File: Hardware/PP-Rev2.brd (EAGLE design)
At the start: 190.5 x 101.3 mm, 181 parts, among them IC1 LT6004, IC2 TLC6C5912-Q1, J1 J_0399700102, Q1 MOSFET-PCHANNEL, Q10 2N7002PW, Q11 2N7002PW, Q12 2N7002PW, Q13 2N7002PW, Q14 2N7002PW, Q15 2N7002PW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

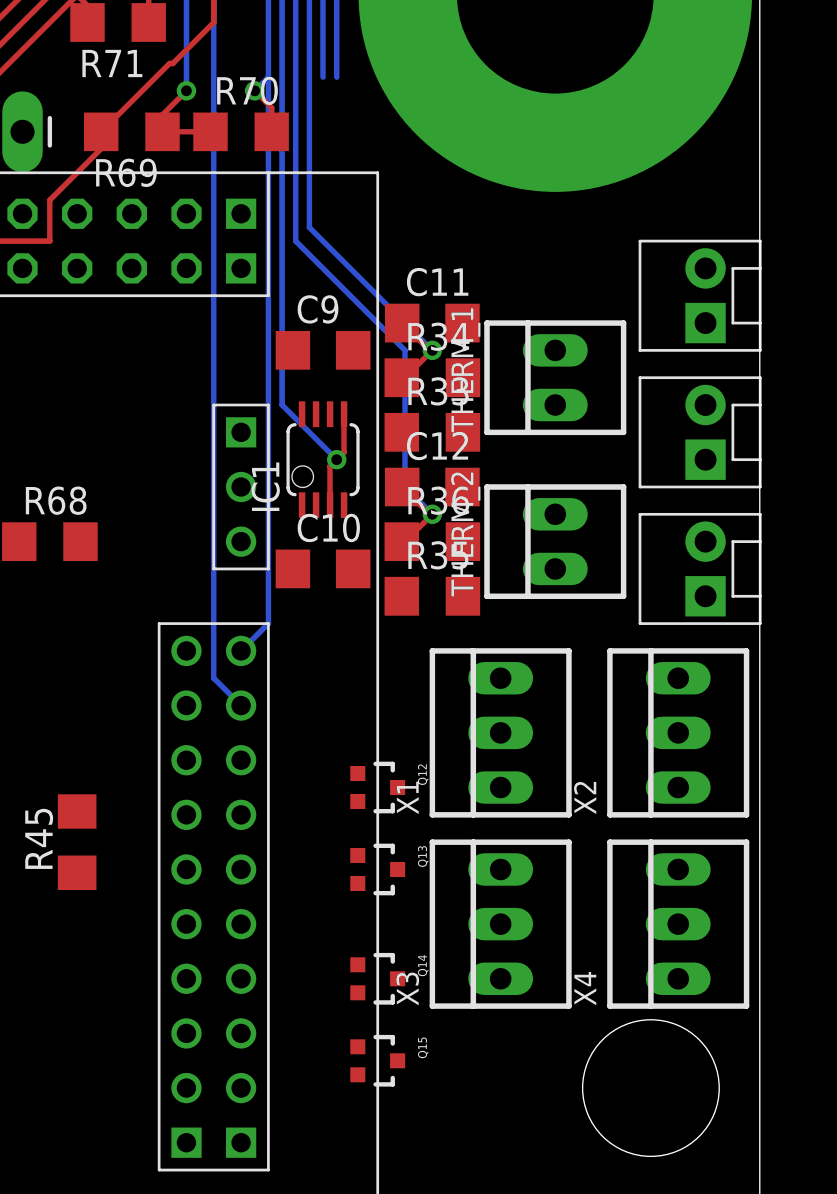
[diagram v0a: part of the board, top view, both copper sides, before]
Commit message: Did most of the fans/temp sensor routing
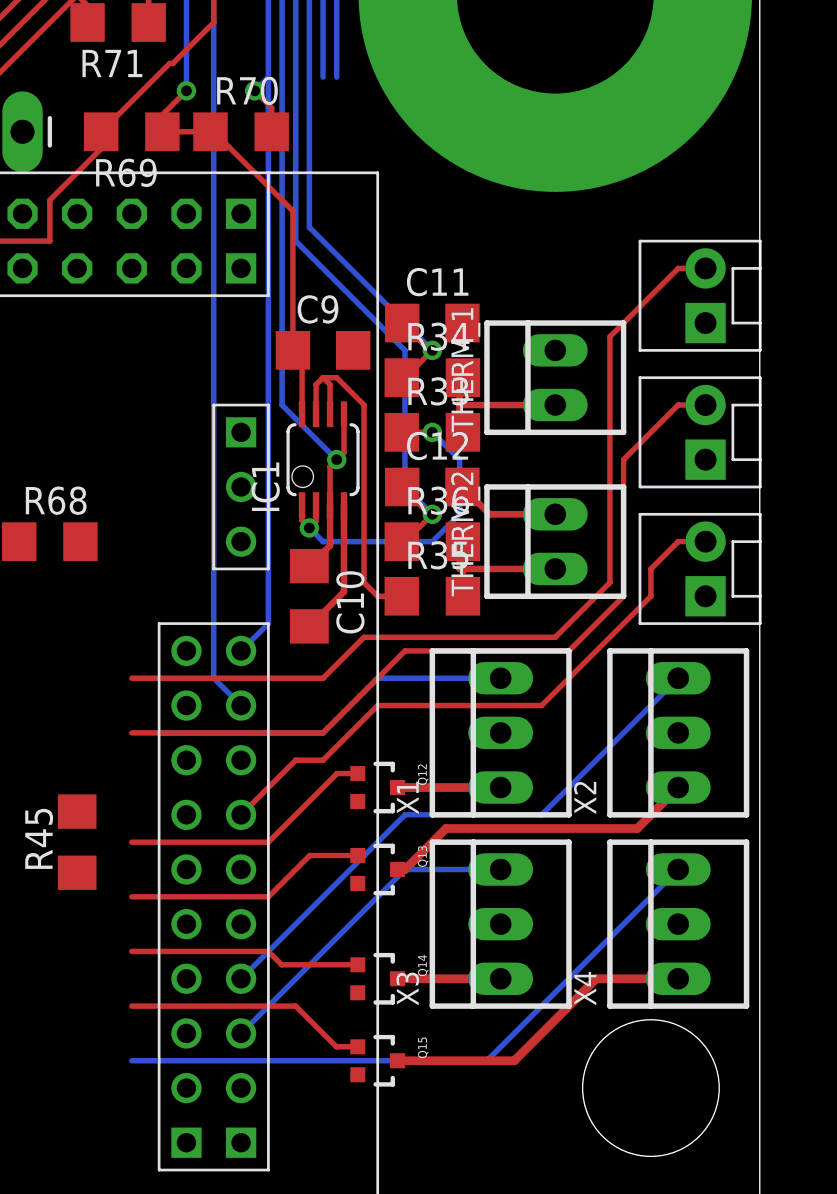
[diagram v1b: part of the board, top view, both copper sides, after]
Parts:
- moved C10 1.42 mm to (169.5, 27.9), turned to 270 degrees
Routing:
- net GAUGE_ON: track 0.00 -> 41.3 mm
- net ESTOP_2: track 0.00 -> 36.7 mm
- net FAN_TACH_4: track 0.00 -> 29.1 mm
- net ESTOP_1: track 0.00 -> 27.6 mm
- net FAN_TACH_2: track 0.00 -> 26.1 mm
- net FAN_TACH_1: track 0.00 -> 16.9 mm
- net N$27: track 0.00 -> 16.4 mm
- net N$25: track 0.00 -> 15.9 mm, vias 0 -> 2
- net FAN_TACH_3: track 0.00 -> 15.2 mm
- net BMS_VREG: track 42.8 -> 57.8 mm
- net N$72: track 0.00 -> 14.6 mm
- net N$70: track 0.00 -> 14.6 mm
- net FAN_CTL_1: track 0.00 -> 11.8 mm
- net FAN_CTL_2: track 0.00 -> 11.3 mm
- net FAN_CTL_4: track 0.00 -> 11.3 mm
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
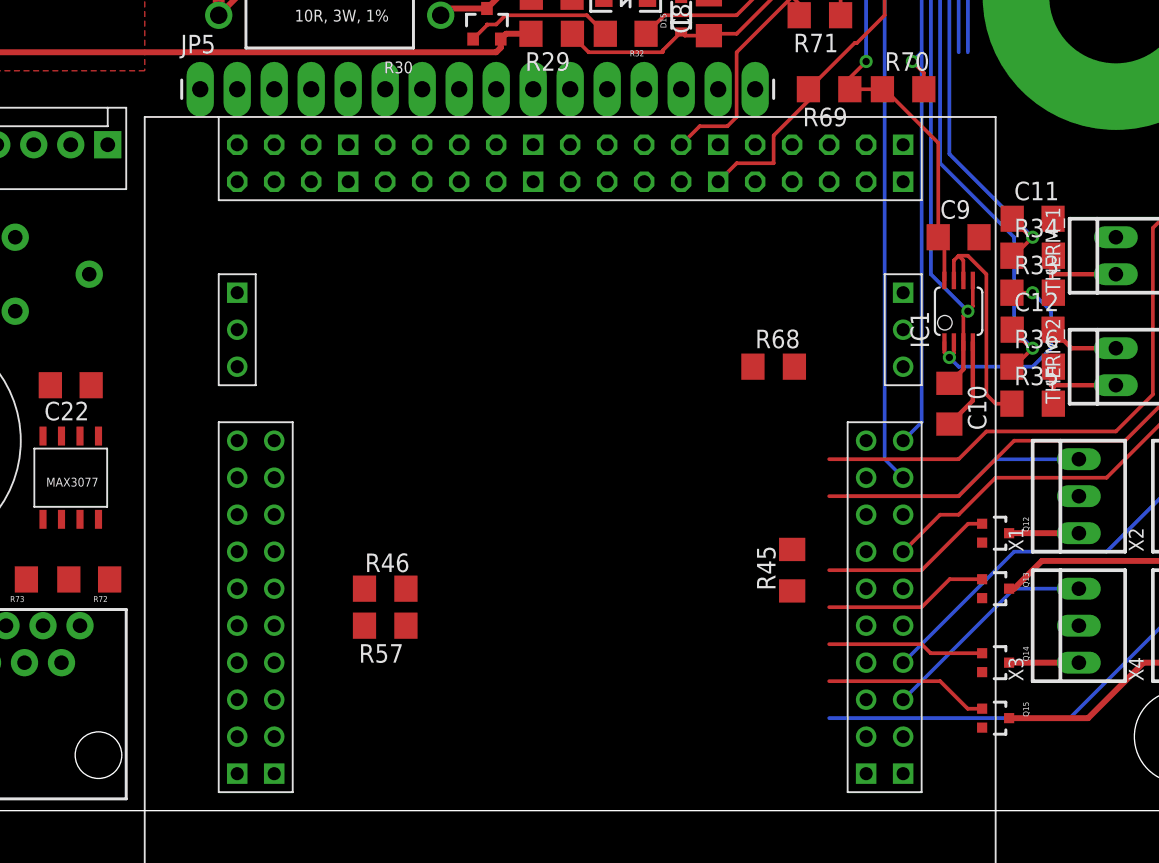
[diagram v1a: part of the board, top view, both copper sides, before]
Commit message: routed most of LCD stuff
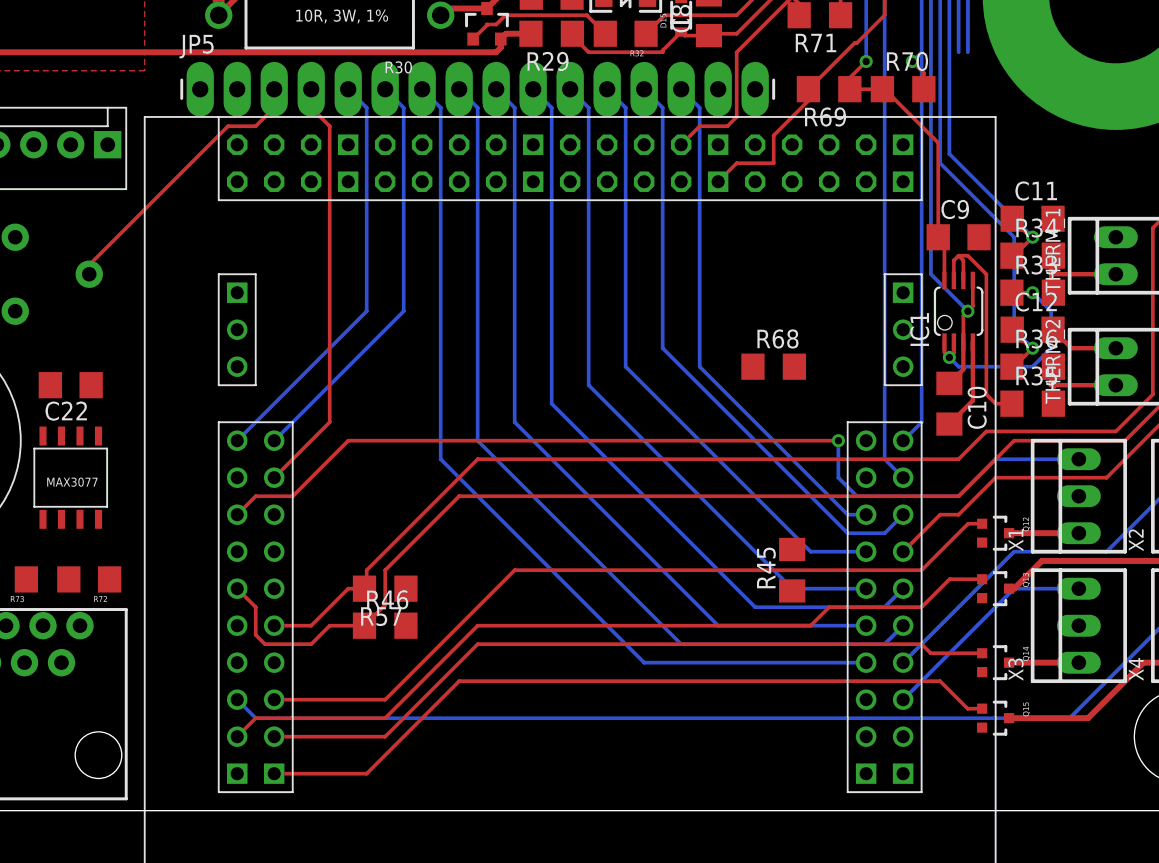
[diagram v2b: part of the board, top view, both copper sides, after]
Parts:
- moved R46 2.54 mm to (130.8, 12.7)
- moved R57 2.54 mm to (130.8, 15.2)
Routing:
- net LCD_DB[0]: track 0.00 -> 60.9 mm
- net LCD_DB[1]: track 0.00 -> 60.2 mm
- net LCD_DB[2]: track 0.00 -> 53.3 mm
- net LCD_DB[3]: track 0.00 -> 52.6 mm
- net ESTOP_2: track 36.7 -> 85.6 mm
- net FAN_TACH_1: track 16.9 -> 64.0 mm, vias 0 -> 1
- net LCD_DB[4]: track 0.00 -> 45.7 mm
- net FAN_CTL_2: track 11.3 -> 55.6 mm
- net GAUGE_ON: track 41.3 -> 84.7 mm
- net FAN_CTL_1: track 11.8 -> 53.6 mm
- net LCD_DB[5]: track 0.00 -> 41.3 mm
- net FAN_TACH_4: track 29.1 -> 70.2 mm
- net FAN_CTL_4: track 11.3 -> 52.0 mm
- net FAN_CTL_3: track 10.8 -> 51.5 mm
- net LCD_DB[6]: track 0.00 -> 40.6 mm
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
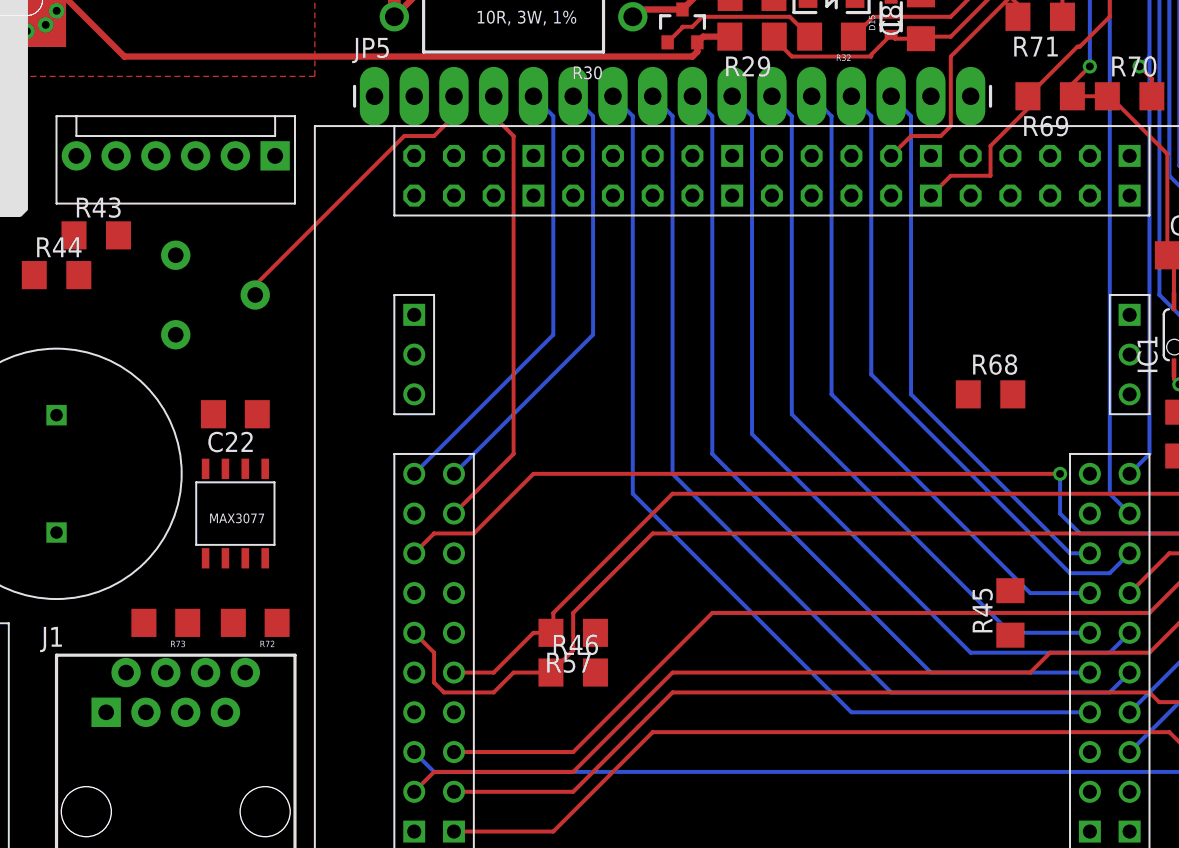
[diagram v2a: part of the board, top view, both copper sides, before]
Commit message: Add stuff for RS-485 transceiver
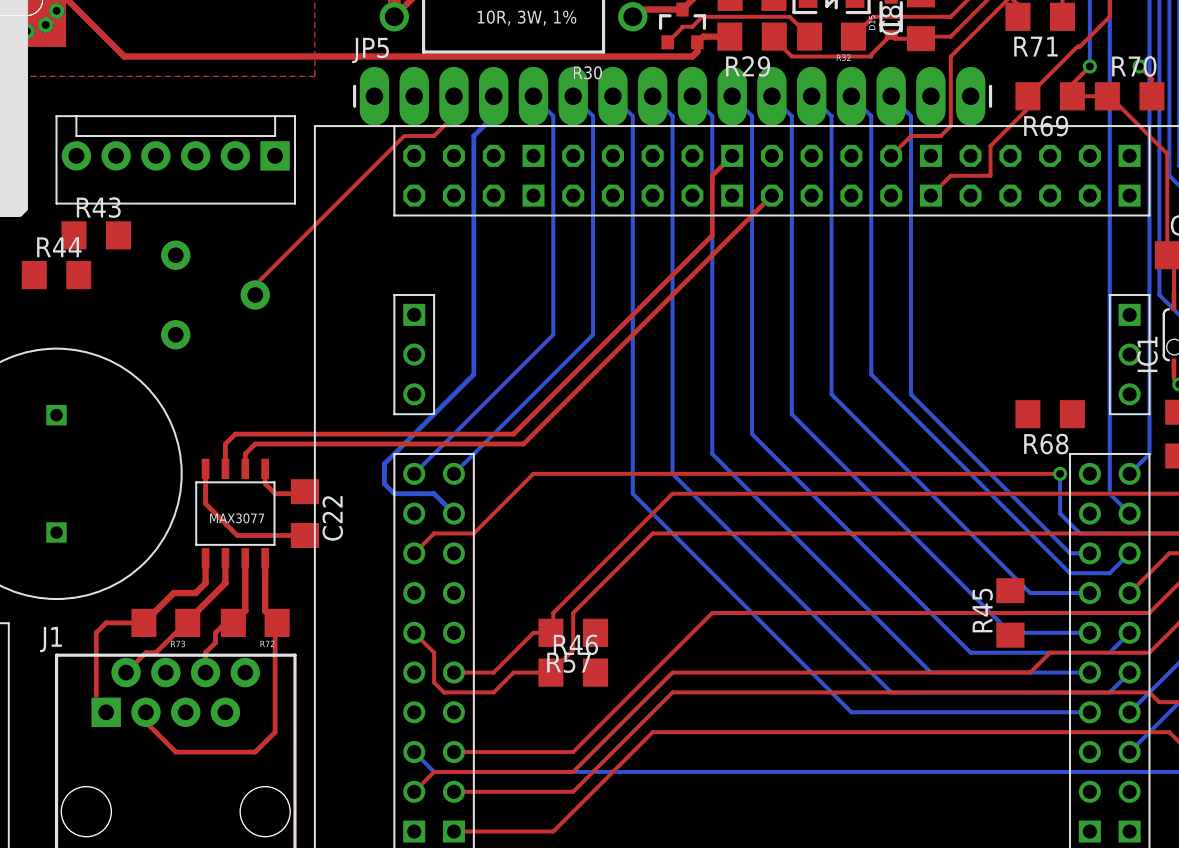
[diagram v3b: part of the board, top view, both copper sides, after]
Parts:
- moved C22 7.75 mm to (113.7, 22.9), turned to 270 degrees
- moved R68 4.02 mm to (161.3, 29.2), turned to 180 degrees
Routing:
- net SER_OUT: track 0.00 -> 43.8 mm
- net SER_IN: track 0.00 -> 41.4 mm
- net N$67: track 0.00 -> 21.7 mm
- net N$35: track 0.00 -> 15.2 mm
- net N$45: track 0.00 -> 10.4 mm
- net GND: track 68.1 -> 77.5 mm
- net N$62: track 0.00 -> 8.65 mm
- net LCD_RS: track 28.8 -> 32.9 mm
- net +5V: track 0.00 -> 3.81 mm

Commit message: Most of the LED stuff routed
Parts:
- moved C15 9.03 mm to (71.1, 32.4), turned to 270 degrees
- moved C16 6.87 mm to (66.0, 33.7), turned to 180 degrees
- moved D20 4.58 mm to (68.6, 36.8)
- moved U$12 4.26 mm to (66.7, 29.2), turned to 180 degrees
- moved C21 3.81 mm to (6.35, 66.0)
- moved R43 0.64 mm to (101.0, 40.6)
- moved IC2 0.63 mm to (12.1, 72.4)
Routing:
- net GAUGE_ON: track 84.7 -> 232.0 mm, vias 0 -> 3
- net LED_SER_IN: track 0.00 -> 144.2 mm, vias 0 -> 4
- net LED_CLR: track 0.00 -> 133.3 mm, vias 0 -> 2
- net LED_SRCK: track 0.00 -> 131.4 mm
- net LED_RCK: track 0.00 -> 125.3 mm
- net PACK_GATE: track 0.00 -> 122.7 mm, vias 0 -> 2
- net CHARGER_CTL: track 0.00 -> 84.5 mm
- net PACK_I_MEAS: track 0.00 -> 84.3 mm, vias 0 -> 2
- net CHARGER_I_MEAS: track 0.00 -> 80.6 mm, vias 0 -> 1
- net N$51: track 0.00 -> 71.6 mm, vias 0 -> 1
- net N$50: track 0.00 -> 63.9 mm, vias 0 -> 1
- net N$49: track 0.00 -> 54.6 mm, vias 0 -> 1
- net SUPPLY_CTL: track 0.00 -> 47.2 mm
- net N$48: track 0.00 -> 46.3 mm, vias 0 -> 1
- net V_CHECK_CHARGER_IN: track 0.00 -> 38.3 mm, vias 0 -> 2
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- added copper zone on layer 1, net CHARGER+
